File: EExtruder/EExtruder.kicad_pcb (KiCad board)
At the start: 2 copper layers, 64.4 x 47.1 mm, 88 parts, among them J1 20A 50V, J11 Conn_01x03_Male, J2 AudioJack4_Ground, J3 6A 50V, J4 6A 50V, J5 Conn_01x02, J6 Conn_01x02, J7 Conn_01x03_Male, J8 Conn_01x03_Male, J9 Conn_01x03_Male, Q1 DTC124E, Q2 PSMN7R0-30YL, Q3 DTC124E, Q4 PSMN7R0-30YL, Q5 SI2318CDS, Q6 SI2318CDS, Q7 SI2318CDS, U1 STM32F030C8Tx, U2 DCBuck, Y1 8MHz

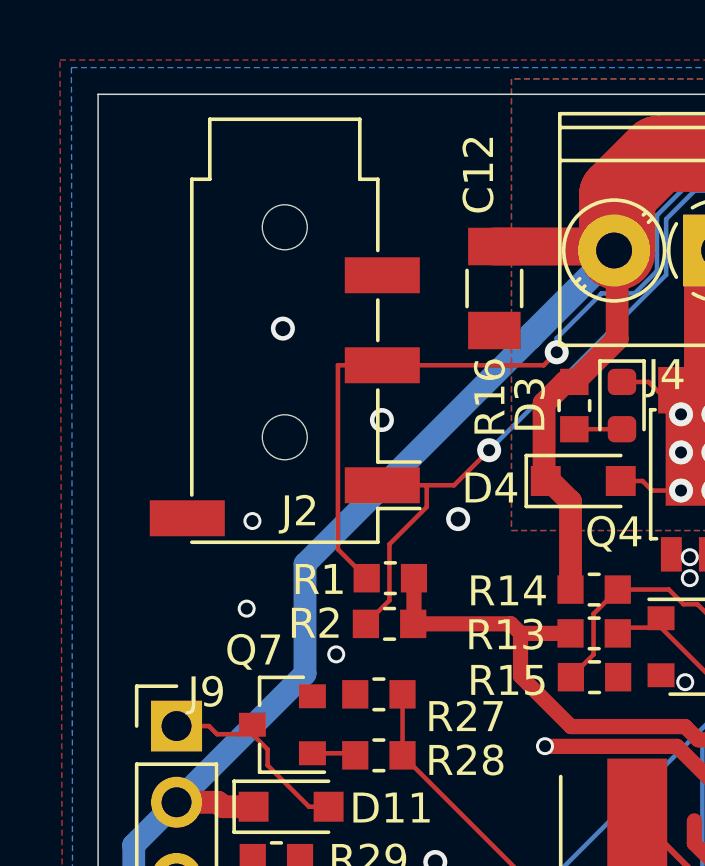
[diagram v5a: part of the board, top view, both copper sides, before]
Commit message: Add solder jumper on the audio jack to avoid ground loops.
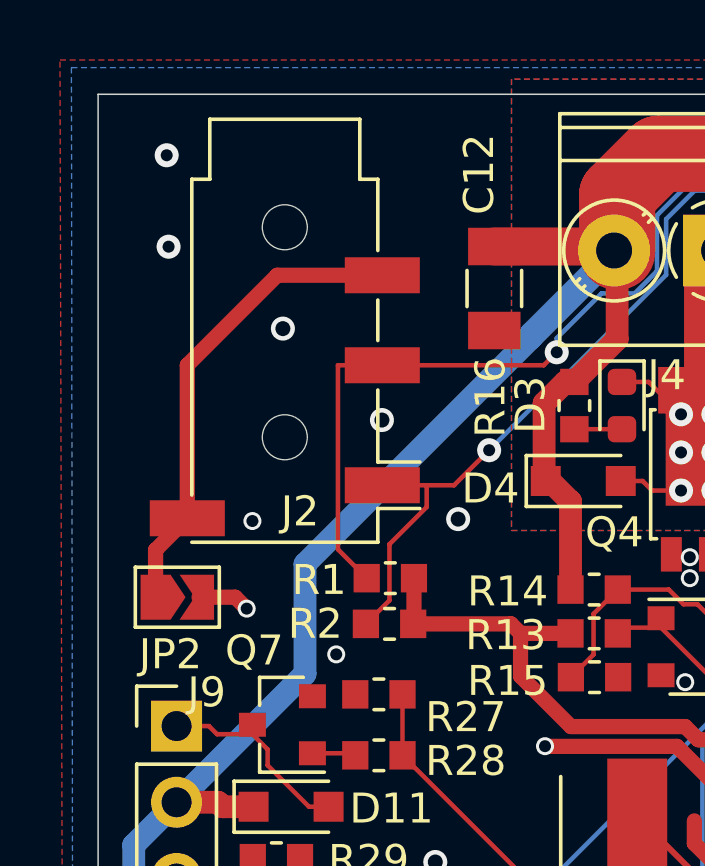
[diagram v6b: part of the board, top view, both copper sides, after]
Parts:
- added JP2: SolderJumper_2_Open, Jumper:SolderJumper-2_P1.3mm_Open_TrianglePad1.0x1.5mm, F.Cu at (130.6, 99.9)
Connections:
- J2 pad R2: GND -> Net-(J2-PadR2)
- J2 pad S: GND -> Net-(J2-PadR2)
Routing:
- net Net-(J2-PadR2): track 0.00 -> 15.9 mm
- net GND: track 45.0 -> 46.8 mm, vias 131 -> 133
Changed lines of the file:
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@@
     (thickness 1.6)
     (drawings 38)
-    (tracks 1070)
+    (tracks 1079)
     (zones 0)
-    (modules 88)
-    (nets 68)
+    (modules 89)
+    (nets 69)
   )
   (page A4)
@@
   )
   (setup
-    (last_trace_width 0.1524)
+    (last_trace_width 0.508)
     (user_trace_width 0.1524)
     (user_trace_width 0.3048)
@@
   (net 66 /~TC0_CS)
   (net 67 /~TC1_CS)
+  (net 68 "Net-(J2-PadR2)")
   (net_class Default "This is the default net class."
     (clearance 0.1524)
@@
     (add_net "Net-(D8-Pad1)")
     (add_net "Net-(D9-Pad2)")
+    (add_net "Net-(J2-PadR2)")
     (add_net "Net-(J7-Pad3)")
     (add_net "Net-(J8-Pad3)")
@@
     (add_net GND)
   )
+  (module Jumper:SolderJumper-2_P1.3mm_Open_TrianglePad1.0x1.5mm (layer F.Cu)
+    (at 130.593 99.8855)
+    (descr "SMD Solder Jumper, 1x1.5mm Triangular Pads, 0.3mm gap, open")
+    (tags "solder jumper open")
+    (attr virtual)
+    (fp_text reference JP2 (at -0.2275 1.905) (layer F.SilkS)
+      (effects (font (size 1 1) (thickness 0.15)))
+    )
+    (fp_text value SolderJumper_2_Open (at 0 1.9) (layer F.Fab)
+      (effects (font (size 1 1) (thickness 0.15)))
+    )
+    (fp_line (start 1.65 1.25) (end -1.65 1.25) (layer F.CrtYd) (width 0.05))
+    (fp_line (start 1.65 1.25) (end 1.65 -1.25) (layer F.CrtYd) (width 0.05))
+    (fp_line (start -1.65 -1.25) (end -1.65 1.25) (layer F.CrtYd) (width 0.05))
+    (fp_line (start -1.65 -1.25) (end 1.65 -1.25) (layer F.CrtYd) (width 0.05))
+    (fp_line (start -1.4 -1) (end 1.4 -1) (layer F.SilkS) (width 0.12))
+    (fp_line (start 1.4 -1) (end 1.4 1) (layer F.SilkS) (width 0.12))
+    (fp_line (start 1.4 1) (end -1.4 1) (layer F.SilkS) (width 0.12))
+    (fp_line (start -1.4 1) (end -1.4 -1) (layer F.SilkS) (width 0.12))
+    (pad 1 smd custom (at -0.725 0) (size 0.3 0.3) (layers F.Cu F.Mask)
+      (net 68 "Net-(J2-PadR2)") (zone_connect 0)
+      (options (clearance outline) (anchor rect))
+      (primitives
+        (gr_poly (pts
+           (xy -0.5 -0.75) (xy 0.5 -0.75) (xy 1 0) (xy 0.5 0.75) (xy -0.5 0.75)
+) (width 0))
+      ))
+    (pad 2 smd custom (at 0.725 0) (size 0.3 0.3) (layers F.Cu F.Mask)
+      (net 1 GND) (zone_connect 0)
+      (options (clearance outline) (anchor rect))
+      (primitives
+        (gr_poly (pts
+           (xy -0.65 -0.75) (xy 0.5 -0.75) (xy 0.5 0.75) (xy -0.65 0.75) (xy -0.15 0)
+) (width 0))
+      ))
+  )
   (module Local:TerminalBlock_Phoenix_PT-1,5-2-3.5-H_1x02_P3.50mm_Horizontal (layer F.Cu)
     (at 148.6535 88.3285 180)
@@
     (pad "" np_thru_hole circle (at -4.775 0 270) (size 1.5 1.5) (drill 1.5) (layers *.Cu *.Mask))
     (pad S smd rect (at -3.175 -3.25 270) (size 1.2 2.5) (layers F.Cu F.Paste F.Mask)
-      (net 1 GND))
+      (net 68 "Net-(J2-PadR2)"))
     (pad R1 smd rect (at -0.175 -3.25 270) (size 1.2 2.5) (layers F.Cu F.Paste F.Mask)
       (net 57 /SDA))
@@
       (net 58 /SCL))
     (pad R2 smd rect (at 4.925 3.25 270) (size 1.2 2.5) (layers F.Cu F.Paste F.Mask)
-      (net 1 GND))
+      (net 68 "Net-(J2-PadR2)"))
     (model ${KISYS3DMOD}/Connector_Audio.3dshapes/Jack_3.5mm_PJ320D_Horizontal.wrl
       (at (xyz 0 0 0))
@@
   (segment (start 155.7147 98.2345) (end 155.580101 98.369099) (width 0.762) (layer F.Cu) (net 1))
   (segment (start 160.1425 98.2345) (end 155.7147 98.2345) (width 0.762) (layer F.Cu) (net 1))
+  (segment (start 132.5245 99.8855) (end 132.9055 100.2665) (width 0.508) (layer F.Cu) (net 1))
+  (segment (start 131.318 99.8855) (end 132.5245 99.8855) (width 0.508) (layer F.Cu) (net 1))
+  (via (at 130.302 88.2015) (size 0.8) (drill 0.4) (layers F.Cu B.Cu) (net 1))
+  (via (at 130.2385 85.1535) (size 0.8) (drill 0.4) (layers F.Cu B.Cu) (net 1))
   (segment (start 153.0345 104.6385) (end 153.0345 106.502) (width 0.508) (layer F.Cu) (net 2))
   (segment (start 153.0345 106.502) (end 153.0855 106.553) (width 0.508) (layer F.Cu) (net 2))
@@
   (segment (start 156.373 113.909778) (end 157.285172 112.997606) (width 0.1524) (layer F.Cu) (net 67))
   (segment (start 156.373 117.126) (end 156.373 113.909778) (width 0.1524) (layer F.Cu) (net 67))
+  (segment (start 130.926 92.1495) (end 130.926 97.254) (width 0.508) (layer F.Cu) (net 68))
+  (segment (start 137.426 89.154) (end 133.9215 89.154) (width 0.508) (layer F.Cu) (net 68))
+  (segment (start 133.9215 89.154) (end 130.926 92.1495) (width 0.508) (layer F.Cu) (net 68))
+  (segment (start 129.868 98.312) (end 129.868 99.8855) (width 0.508) (layer F.Cu) (net 68))
+  (segment (start 130.926 97.254) (end 129.868 98.312) (width 0.508) (layer F.Cu) (net 68))
   (zone (net 13) (net_name "Net-(D3-Pad1)") (layer B.Cu) (hatch edge 0.508)
     (priority 1)
